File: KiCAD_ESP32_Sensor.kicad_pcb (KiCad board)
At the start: 2 copper layers, 50 x 40 mm, 24 parts, among them J1 USB_C_Receptacle_USB2.0_16P, J2 VL53L0X_Module, Q1 MMBT3904, Q2 MMBT3904, U1 CH340C, U2 AMS1117-3.3, U3 ESP32-WROOM-32E

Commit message: Finished rough PCB design, will finalize later
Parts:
- moved R5 72.6 mm to (55.9, 59.1), turned to 180 degrees
- moved C9 70.7 mm to (55.9, 57.0), turned to 180 degrees
- moved C8 70.4 mm to (55.9, 54.8), turned to 180 degrees
- moved C7 70.2 mm to (55.9, 52.7), turned to 180 degrees
- moved C6 68.8 mm to (55.0, 62.1), turned to 90 degrees
- moved R4 51.9 mm to (81.6, 85.3), turned to -90 degrees
- moved R8 47.1 mm to (81.4, 79.8), turned to -90 degrees
- moved R7 47.0 mm to (81.4, 75.8), turned to 90 degrees
- moved R6 39.5 mm to (79.3, 70.3)
- moved J2 16.0 mm to (80.6, 52.8)
- moved C2 15.7 mm to (67.7, 75.7)
- moved C1 15.6 mm to (67.7, 77.9)
- moved R3 8.53 mm to (68.5, 86.3)
- moved U3 7.27 mm to (67.7, 56.6)
- moved Q1 2.42 mm to (55.2, 72.9)
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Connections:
- C7 pad 2: Net-(C7-Pad2) -> GND
- C9 pad 2: Net-(C7-Pad2) -> GND
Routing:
- net +3.3V: track 0.14 -> 130.0 mm, vias 0 -> 10
- net RXD: track 0.00 -> 35.0 mm, vias 0 -> 2
- net TXD: track 0.00 -> 34.9 mm, vias 0 -> 2
- net GND: track 0.00 -> 31.0 mm, vias 0 -> 5
- net EN: track 0.00 -> 27.3 mm, vias 0 -> 2
- net DTR: track 0.00 -> 24.9 mm, vias 0 -> 2
- net IO0: track 0.00 -> 24.8 mm, vias 0 -> 2
- net SCL: track 0.00 -> 23.4 mm
- net +5V: track 0.00 -> 21.2 mm, vias 0 -> 2
- net RTS: track 0.00 -> 20.8 mm, vias 0 -> 2
- net SDA: track 0.00 -> 18.4 mm
- net USB_D_MINUS: track 0.00 -> 9.78 mm, vias 0 -> 2
- net Net-(J1-CC1): track 0.00 -> 8.29 mm
- net Net-(J1-CC2): track 0.00 -> 6.96 mm
- net USB_D_PLUS: track 0.00 -> 6.33 mm
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- added copper zone on F.Cu, net GND
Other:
- board size 50 x 40 mm -> 31.7 x 40 mm

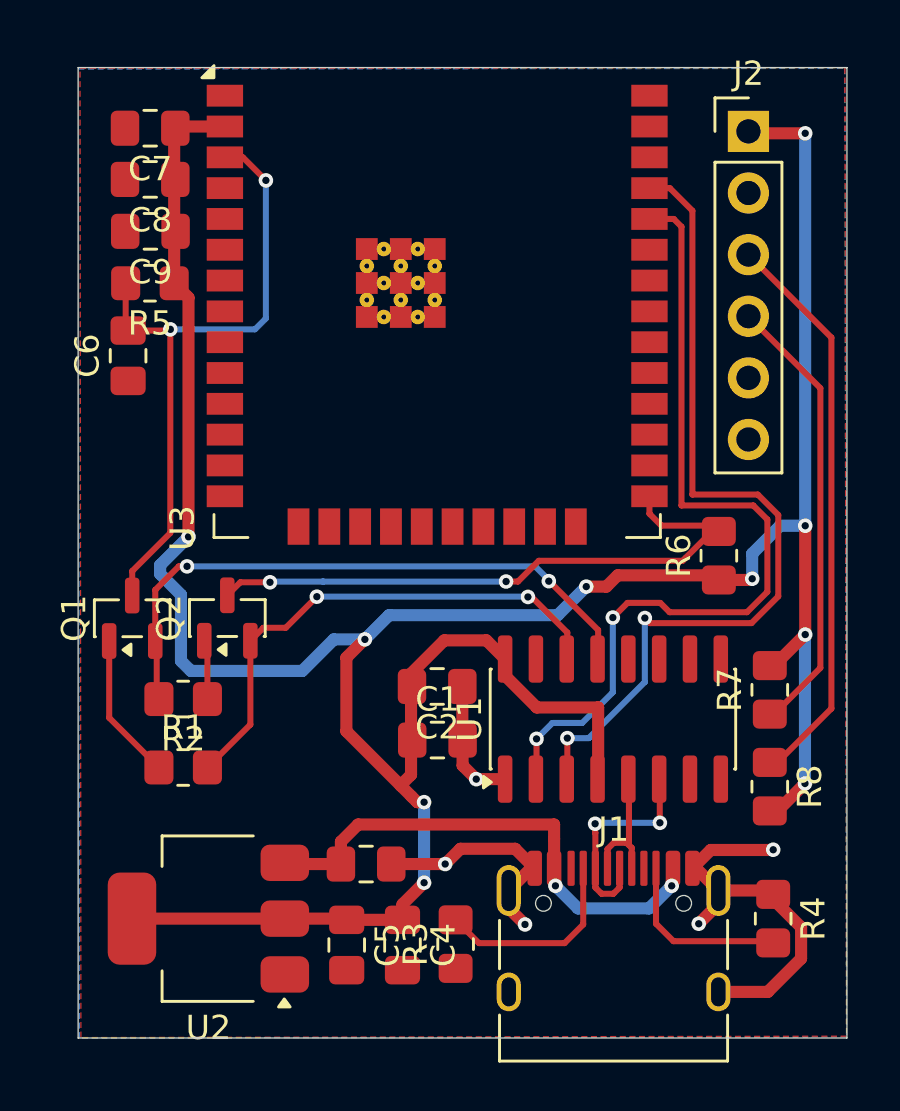
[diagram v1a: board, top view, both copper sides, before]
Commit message: Full PCB design V1.0 completed, will update with changes soon.
Will do some major changes including:
Replacing the MCU with a more modern ESP32, smaller, use PBs on the board, etc.
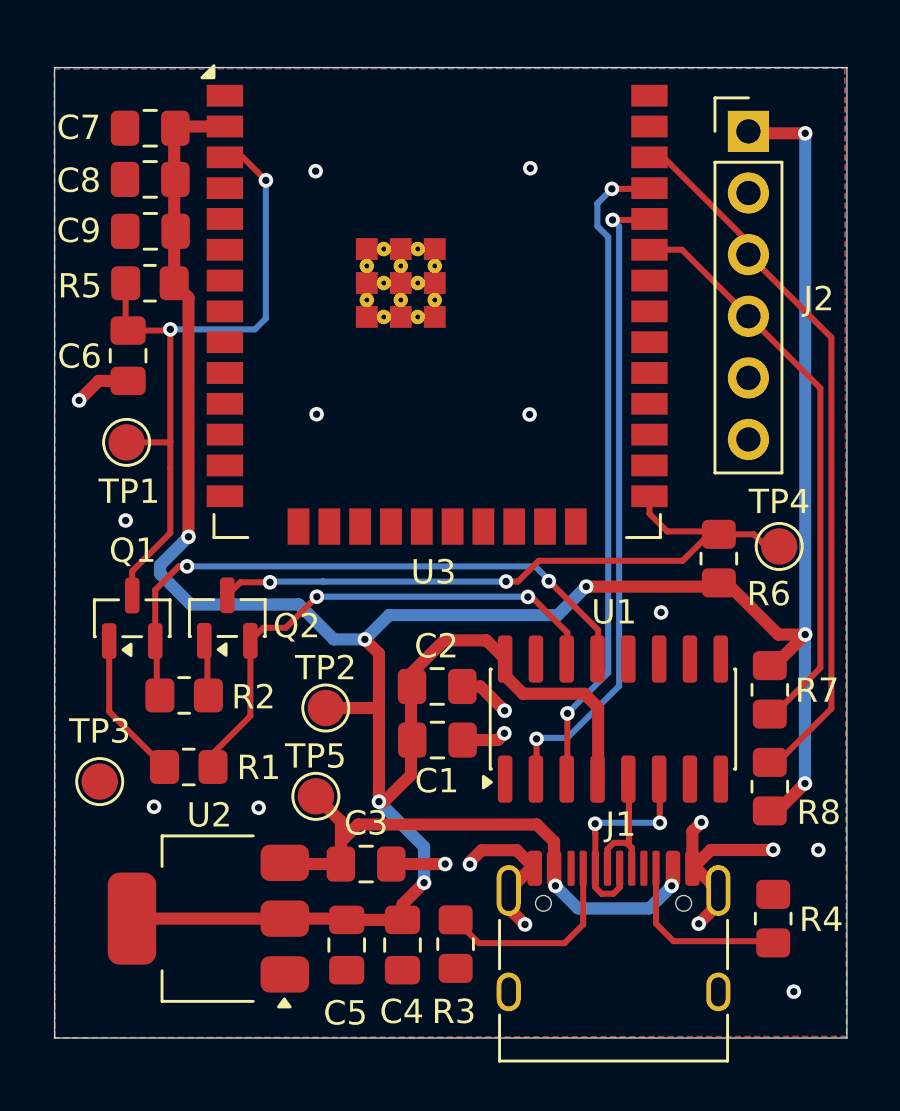
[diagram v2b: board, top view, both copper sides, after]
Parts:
- added TP1: TestPoint, TestPoint:TestPoint_Pad_D1.5mm, F.Cu at (54.9, 65.7)
- added TP2: TestPoint, TestPoint:TestPoint_Pad_D1.5mm, F.Cu at (63.1, 76.6)
- added TP3: TestPoint, TestPoint:TestPoint_Pad_D1.5mm, F.Cu at (53.8, 79.6)
- added TP4: TestPoint, TestPoint:TestPoint_Pad_D1.5mm, F.Cu at (81.8, 69.9)
- added TP5: TestPoint, TestPoint:TestPoint_Pad_D1.5mm, F.Cu at (62.7, 80.2)
- moved R1 0.23 mm to (57.5, 79.0)
- moved R2 0.16 mm to (57.3, 76.1)
- moved R6 0.12 mm to (79.3, 70.4)
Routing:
- net TXD: track 34.9 -> 26.1 mm
- net RXD: track 35.0 -> 26.3 mm
- net GND: track 31.0 -> 22.5 mm, vias 5 -> 19
- net SDA: track 18.4 -> 23.6 mm
- net SCL: track 23.4 -> 28.3 mm
- net +3.3V: track 130.0 -> 126.8 mm, vias 10 -> 8
- net IO0: track 24.8 -> 27.5 mm
- net +5V: track 21.2 -> 23.0 mm
- net EN: track 27.3 -> 29.0 mm
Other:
- board size 31.7 x 40 mm -> 32.7 x 40 mm
